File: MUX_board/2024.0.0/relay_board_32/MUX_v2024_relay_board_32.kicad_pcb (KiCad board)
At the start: 2 copper layers, 140 x 350 mm, 192 parts, among them K1 G5LE-1-VD, K10 G5LE-1-VD, K11 G5LE-1-VD, K12 G5LE-1-VD, K13 G5LE-1-VD, K14 G5LE-1-VD, K15 G5LE-1-VD, K16 G5LE-1-VD, K17 G5LE-1-VD, K18 G5LE-1-VD, K19 G5LE-1-VD, K2 G5LE-1-VD, K20 G5LE-1-VD, K21 G5LE-1-VD, K22 G5LE-1-VD, K23 G5LE-1-VD, K24 G5LE-1-VD, K25 G5LE-1-VD, K26 G5LE-1-VD, K27 G5LE-1-VD, K28 G5LE-1-VD, K29 G5LE-1-VD, K3 G5LE-1-VD, K30 G5LE-1-VD, K31 G5LE-1-VD, K32 G5LE-1-VD, K4 G5LE-1-VD, K5 G5LE-1-VD, K6 G5LE-1-VD, K7 G5LE-1-VD, K8 G5LE-1-VD, K9 G5LE-1-VD, Q1 STP16NF06L, Q10 STP16NF06L, Q11 STP16NF06L, Q12 STP16NF06L, Q13 STP16NF06L, Q14 STP16NF06L, Q15 STP16NF06L, Q16 STP16NF06L, Q17 STP16NF06L, Q18 STP16NF06L, Q19 STP16NF06L, Q2 STP16NF06L, Q20 STP16NF06L, Q21 STP16NF06L, Q22 STP16NF06L, Q23 STP16NF06L, Q24 STP16NF06L, Q25 STP16NF06L, Q26 STP16NF06L, Q27 STP16NF06L, Q28 STP16NF06L, Q29 STP16NF06L, Q3 STP16NF06L, Q30 STP16NF06L, Q31 STP16NF06L, Q32 STP16NF06L, Q4 STP16NF06L, Q5 STP16NF06L, Q6 STP16NF06L, Q7 STP16NF06L, Q8 STP16NF06L, Q9 STP16NF06L, U1 MCP23017_SP, U2 MCP23017_SP

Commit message: Updates footprints
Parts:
- Electrodes: footprint TerminalBlock_Phoenix:TerminalBlock_Phoenix_MKDS-1,5-16_1x16_P5.00mm_Horizontal -> TerminalBlock_Phoenix:TerminalBlock_Phoenix_MKDS-1,5-16-5.08_1x16_P5.08mm_Horizontal
- GND  PWR: footprint TerminalBlock_Phoenix:TerminalBlock_Phoenix_MKDS-1,5-2_1x02_P5.00mm_Horizontal -> TerminalBlock_Phoenix:TerminalBlock_Phoenix_MKDS-1,5-2-5.08_1x02_P5.08mm_Horizontal
- x  y  xx yy: footprint TerminalBlock_Phoenix:TerminalBlock_Phoenix_MKDS-1,5-4_1x04_P5.00mm_Horizontal -> TerminalBlock_Phoenix:TerminalBlock_Phoenix_MKDS-1,5-4-5.08_1x04_P5.08mm_Horizontal
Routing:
- net 12V: track 1166.4 -> 1150.6 mm
- net Role xx: track 358.3 -> 343.8 mm
- net Electrode 11: track 339.2 -> 325.6 mm
- net Role x: track 404.3 -> 398.5 mm
- net SCL1: track 68.7 -> 65.1 mm
- net Electrode 9: track 428.1 -> 424.7 mm
- net Electrode 1: track 112.4 -> 115.4 mm
- net Electrode 15: track 129.1 -> 127.7 mm
- net Electrode 2: track 149.3 -> 150.5 mm
- net Electrode 4: track 225.3 -> 226.2 mm
- net Electrode 6: track 301.1 -> 301.9 mm
- net Role y: track 409.7 -> 409.0 mm
- net Electrode 5: track 311.6 -> 312.3 mm
- net Electrode 8: track 419.1 -> 419.7 mm
- net Electrode 13: track 228.1 -> 227.5 mm
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
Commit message: Adds pull up on MCP
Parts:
- added R33: 10k, Resistor_THT:R_Axial_DIN0207_L6.3mm_D2.5mm_P15.24mm_Horizontal, F.Cu at (107.4, 372.8)
- added R34: 10k, Resistor_THT:R_Axial_DIN0207_L6.3mm_D2.5mm_P15.24mm_Horizontal, F.Cu at (102.5, 372.8)
- moved Jumper 5V 15.5 mm to (104.9, 348.4)
- moved Jumper E8 6.50 mm to (105.0, 365.1)
- moved Jumper x 0.50 mm to (150.0, 61.8)
- moved Jumper y 0.50 mm to (150.0, 44.8)
- moved Addr1 0.10 mm to (110.3, 378.9)
- moved Addr2 0.10 mm to (115.7, 378.9)
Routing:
- net SD1: track 47.5 -> 66.3 mm
- net +5V: track 112.0 -> 127.2 mm
- net Electrode 9: track 424.7 -> 419.9 mm
- net SCL1: track 65.1 -> 68.3 mm
- net Electrode 8: track 419.7 -> 422.1 mm
- net Electrode 1: track 115.4 -> 113.6 mm
- net 12V: track 1150.6 -> 1152.1 mm
- net Role y: track 409.0 -> 408.4 mm

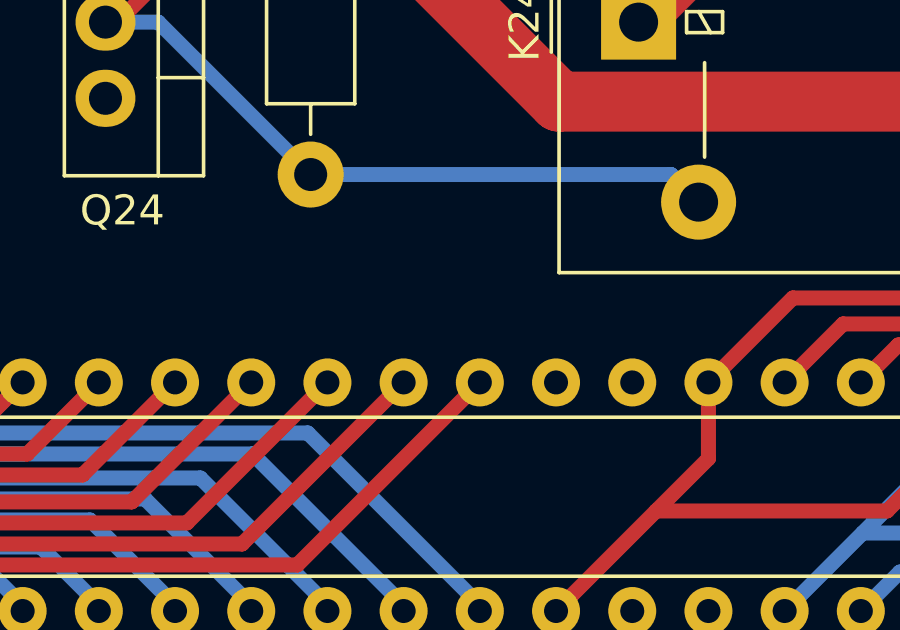
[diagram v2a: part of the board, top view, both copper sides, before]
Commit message: Adds capacitor on MCP
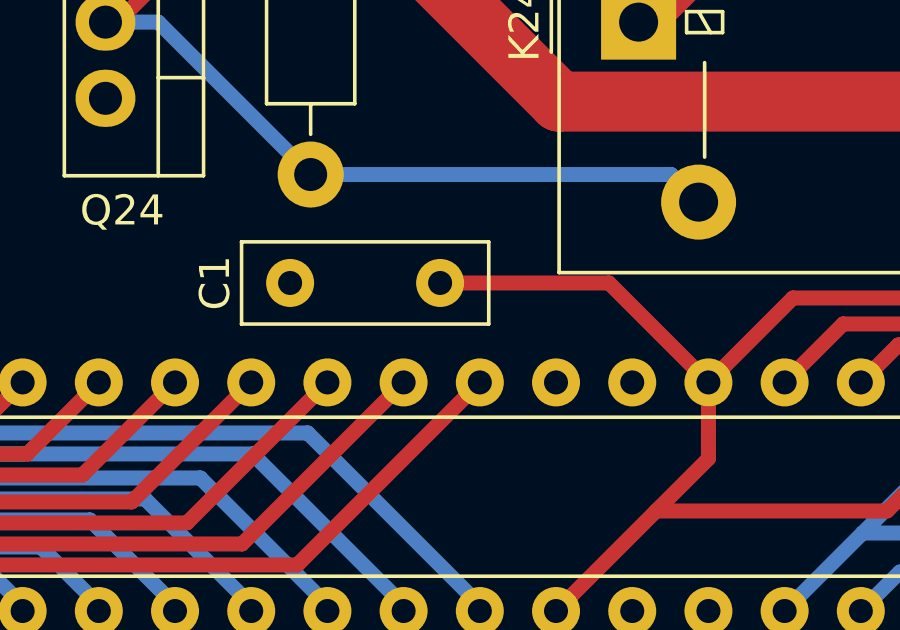
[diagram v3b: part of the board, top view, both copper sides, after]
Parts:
- added C1: 100nF, Capacitor_THT:C_Disc_D8.0mm_W2.5mm_P5.00mm, F.Cu at (68.0, 374.0)
- R33, R34: value 10k -> 100k
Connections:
- R33 pad 1: SD1 -> +5V
- R33 pad 2: +5V -> SD1
- R34 pad 1: SCL1 -> +5V
- R34 pad 2: +5V -> SCL1
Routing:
- net +5V: track 127.2 -> 137.5 mm
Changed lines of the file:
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@@
     )
   )
+  (footprint "Capacitor_THT:C_Disc_D8.0mm_W2.5mm_P5.00mm" (layer "F.Cu")
+    (at 68 374 180)
+    (descr "C, Disc series, Radial, pin pitch=5.00mm, , diameter*width=8*2.5mm^2, Capacitor, http://cdn-reichelt.de/documents/datenblatt/B300/DS_KERKO_TC.pdf")
+    (tags "C Disc series Radial pin pitch 5.00mm  diameter 8mm width 2.5mm Capacitor")
+    (property "Sheetfile" "MUX_v2024_relay_board_32.kicad_sch")
+    (property "Sheetname" "")
+    (attr through_hole)
+    (fp_text reference "C1" (at 7.5 0 90) (layer "F.SilkS")
+      (effects (font (size 1 1) (thickness 0.15)))
+    )
+    (fp_text value "100nF" (at 2.5 2.5) (layer "F.Fab")
+      (effects (font (size 1 1) (thickness 0.15)))
+    )
+    (fp_text user "${REFERENCE}" (at 2.5 0) (layer "F.Fab")
+      (effects (font (size 1 1) (thickness 0.15)))
+    )
+    (fp_line (start -1.62 1.37) (end 6.62 1.37) (layer "F.SilkS") (width 0.12))
+    (fp_line (start -1.62 -1.37) (end 6.62 -1.37) (layer "F.SilkS") (width 0.12))
+    (fp_line (start -1.62 -1.37) (end -1.62 1.37) (layer "F.SilkS") (width 0.12))
+    (fp_line (start 6.62 -1.37) (end 6.62 1.37) (layer "F.SilkS") (width 0.12))
+    (fp_line (start -1.75 -1.5) (end -1.75 1.5) (layer "F.CrtYd") (width 0.05))
+    (fp_line (start 6.75 -1.5) (end -1.75 -1.5) (layer "F.CrtYd") (width 0.05))
+    (fp_line (start 6.75 1.5) (end 6.75 -1.5) (layer "F.CrtYd") (width 0.05))
+    (fp_line (start -1.75 1.5) (end 6.75 1.5) (layer "F.CrtYd") (width 0.05))
+    (fp_line (start -1.5 -1.25) (end -1.5 1.25) (layer "F.Fab") (width 0.1))
+    (fp_line (start -1.5 1.25) (end 6.5 1.25) (layer "F.Fab") (width 0.1))
+    (fp_line (start 6.5 1.25) (end 6.5 -1.25) (layer "F.Fab") (width 0.1))
+    (fp_line (start 6.5 -1.25) (end -1.5 -1.25) (layer "F.Fab") (width 0.1))
+    (pad "1" thru_hole circle (at 0 0 180) (size 1.6 1.6) (drill 0.8) (layers *.Cu *.Mask)
+      (net 23 "+5V") (pintype "passive"))
+    (pad "2" thru_hole circle (at 5 0 180) (size 1.6 1.6) (drill 0.8) (layers *.Cu *.Mask)
+      (net 18 "GND") (pintype "passive"))
+    (model "${KICAD6_3DMODEL_DIR}/Capacitor_THT.3dshapes/C_Disc_D8.0mm_W2.5mm_P5.00mm.wrl"
+      (offset (xyz 0 0 0))
+      (scale (xyz 1 1 1))
+      (rotate (xyz 0 0 0))
+    )
+  )
   (footprint "Package_TO_SOT_THT:TO-220-3_Vertical" (layer "F.Cu")
     (at 56.845 159.576664 -90)
@@
       (effects (font (size 1 1) (thickness 0.15)))
     )
-    (fp_text value "10k" (at 7.62 2.37 90) (layer "F.Fab")
+    (fp_text value "100k" (at 7.62 2.37 90) (layer "F.Fab")
       (effects (font (size 1 1) (thickness 0.15)))
     )
@@
     (fp_line (start 0 0) (end 4.47 0) (layer "F.Fab") (width 0.1))
     (pad "1" thru_hole circle (at 0 0 90) (size 1.6 1.6) (drill 0.8) (layers *.Cu *.Mask)
-      (net 19 "SCL1") (pintype "passive"))
-    (pad "2" thru_hole oval (at 15.24 0 90) (size 1.6 1.6) (drill 0.8) (layers *.Cu *.Mask)
       (net 23 "+5V") (pintype "passive"))
+    (pad "2" thru_hole oval (at 15.24 0 90) (size 1.6 1.6) (drill 0.8) (layers *.Cu *.Mask)
+      (net 19 "SCL1") (pintype "passive"))
     (model "${KICAD6_3DMODEL_DIR}/Resistor_THT.3dshapes/R_Axial_DIN0207_L6.3mm_D2.5mm_P15.24mm_Horizontal.wrl"
       (offset (xyz 0 0 0))
@@
       (effects (font (size 1 1) (thickness 0.15)))
     )
-    (fp_text value "10k" (at 7.62 2.37 90) (layer "F.Fab")
+    (fp_text value "100k" (at 7.62 2.37 90) (layer "F.Fab")
       (effects (font (size 1 1) (thickness 0.15)))
     )
@@
     (fp_line (start 0 0) (end 4.47 0) (layer "F.Fab") (width 0.1))
     (pad "1" thru_hole circle (at 0 0 90) (size 1.6 1.6) (drill 0.8) (layers *.Cu *.Mask)
-      (net 21 "SD1") (pintype "passive"))
-    (pad "2" thru_hole oval (at 15.24 0 90) (size 1.6 1.6) (drill 0.8) (layers *.Cu *.Mask)
       (net 23 "+5V") (pintype "passive"))
+    (pad "2" thru_hole oval (at 15.24 0 90) (size 1.6 1.6) (drill 0.8) (layers *.Cu *.Mask)
+      (net 21 "SD1") (pintype "passive"))
     (model "${KICAD6_3DMODEL_DIR}/Resistor_THT.3dshapes/R_Axial_DIN0207_L6.3mm_D2.5mm_P15.24mm_Horizontal.wrl"
       (offset (xyz 0 0 0))
@@
   (segment (start 75.19875 381.6) (end 76.94375 379.855) (width 0.5) (layer "F.Cu") (net 23))
   (segment (start 76.94375 377.315) (end 79.75875 374.5) (width 0.5) (layer "F.Cu") (net 23))
+  (segment (start 73.62875 374) (end 68 374) (width 0.5) (layer "F.Cu") (net 23))
   (segment (start 115.700625 383.975) (end 116.680625 384.955) (width 0.5) (layer "F.Cu") (net 23))
   (segment (start 98.55 378.1) (end 86.4 378.1) (width 0.5) (layer "F.Cu") (net 23))
+  (segment (start 76.94375 377.315) (end 73.62875 374) (width 0.5) (layer "F.Cu") (net 23))
   (segment (start 104.425 383.975) (end 98.55 378.1) (width 0.5) (layer "F.Cu") (net 23))
   (segment (start 107.4 357.6) (end 105.4 357.6) (width 0.5) (layer "F.Cu") (net 23))
